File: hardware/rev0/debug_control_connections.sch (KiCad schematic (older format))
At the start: 1 part, among them IC1 ECP5-BGA256

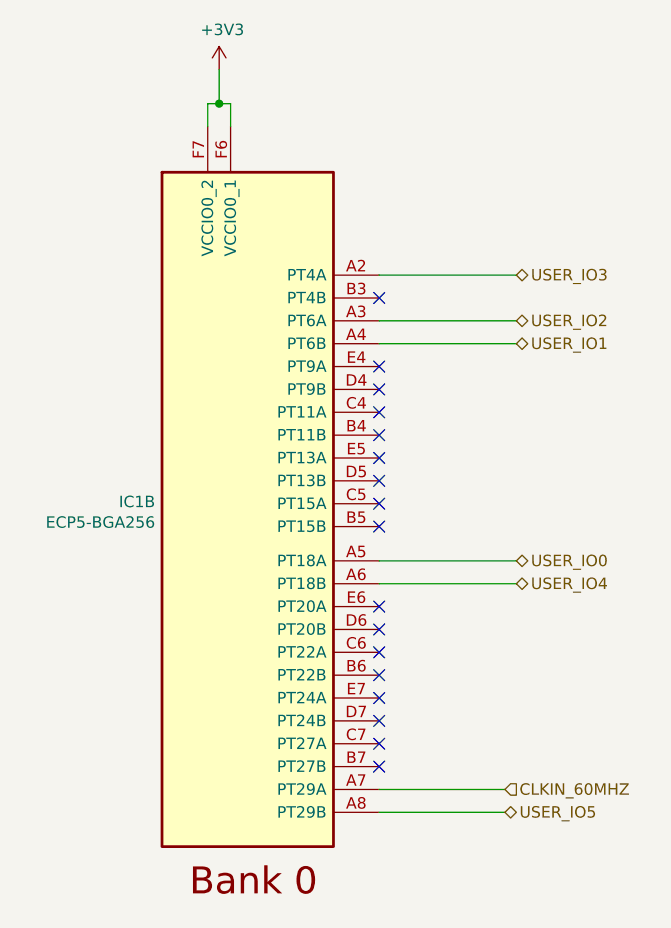
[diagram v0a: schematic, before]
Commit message: Route LVDS user IO
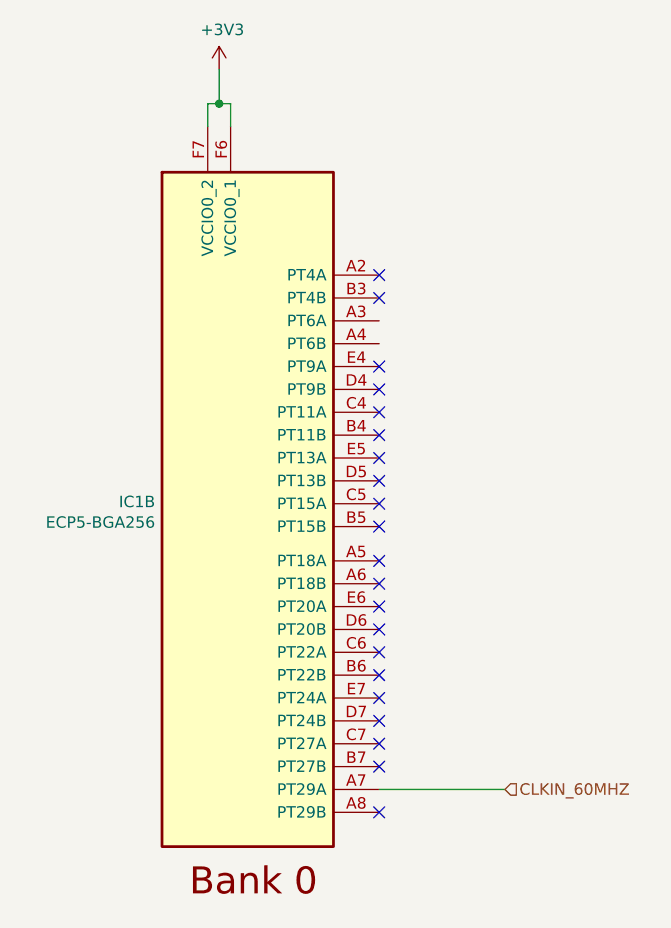
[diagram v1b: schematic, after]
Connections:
- net USER_IO0: no longer names the net of IC1.A5 (PT18A)
- net USER_IO1: no longer names the net of IC1.A4 (PT6B)
- net USER_IO2: no longer names the net of IC1.A3 (PT6A)
- net USER_IO3: no longer names the net of IC1.A2 (PT4A)
- net USER_IO4: no longer names the net of IC1.A6 (PT18B)
- net USER_IO5: no longer names the net of IC1.A8 (PT29B)
- no-connect marks 17 -> 21
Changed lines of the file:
@@
 $EndComp
 Wire Wire Line
-	3150 2400 3750 2400
-Wire Wire Line
-	3150 2600 3750 2600
-Wire Wire Line
-	3150 2700 3750 2700
-Wire Wire Line
-	3150 3650 3750 3650
-Wire Wire Line
-	3150 3750 3750 3750
-Text HLabel 3750 3650 2    50   BiDi ~ 0
-USER_IO0
-Text HLabel 3750 2700 2    50   BiDi ~ 0
-USER_IO1
-Text HLabel 3750 2600 2    50   BiDi ~ 0
-USER_IO2
-Text HLabel 3750 2400 2    50   BiDi ~ 0
-USER_IO3
-Text HLabel 3750 3750 2    50   BiDi ~ 0
-USER_IO4
-Wire Wire Line
-	3150 4750 3700 4750
-Text HLabel 3700 4750 2    50   BiDi ~ 0
-USER_IO5
-Wire Wire Line
 	3150 4650 3700 4650
+NoConn ~ 3150 2400
+NoConn ~ 3150 3650
+NoConn ~ 3150 3750
+NoConn ~ 3150 4750
 $EndSCHEMATC

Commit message: Route/NC remaining target signals, ERC & schematic cleanup
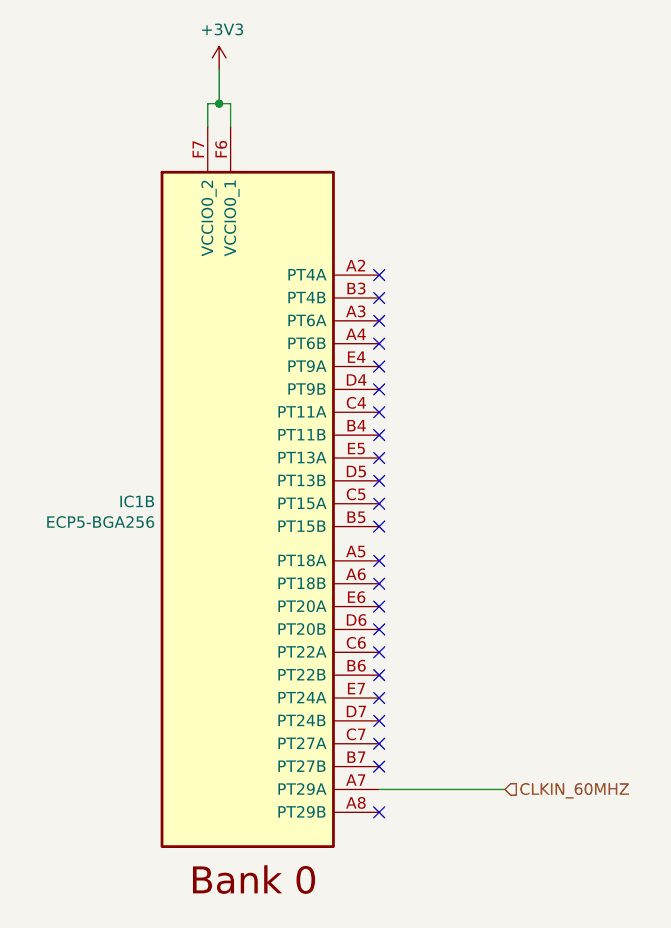
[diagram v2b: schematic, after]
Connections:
- no-connect marks 21 -> 23
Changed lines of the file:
@@
 NoConn ~ 3150 3750
 NoConn ~ 3150 4750
+NoConn ~ 3150 2600
+NoConn ~ 3150 2700
 $EndSCHEMATC
